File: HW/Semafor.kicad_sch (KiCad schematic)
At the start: 62 parts, among them J1 USB_C_Receptacle_USB2.0, J2 USB_plug, M1 Motor_DC, Q3 Q_NMOS_GSD, Q4 Q_NMOS_GSD, SW6 SW_SPDT, U1 ESP32-C3, U2 CN3058E, U3 LT1930, U4 E22-900T22D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

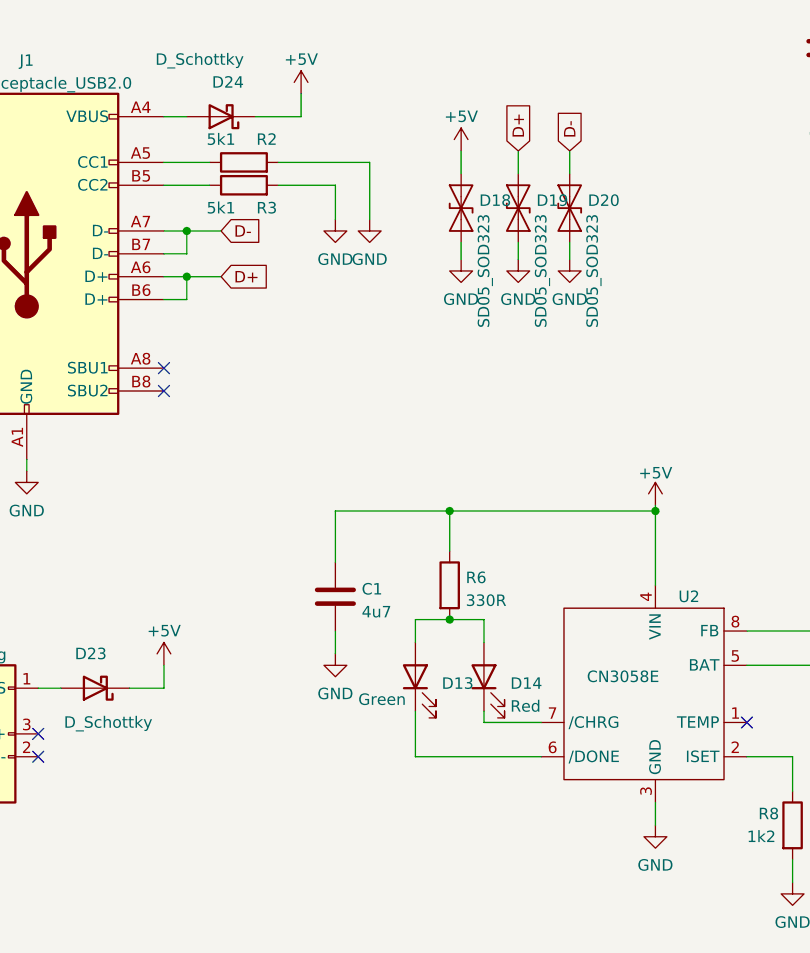
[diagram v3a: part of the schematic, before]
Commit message: routing PCB - LEDs
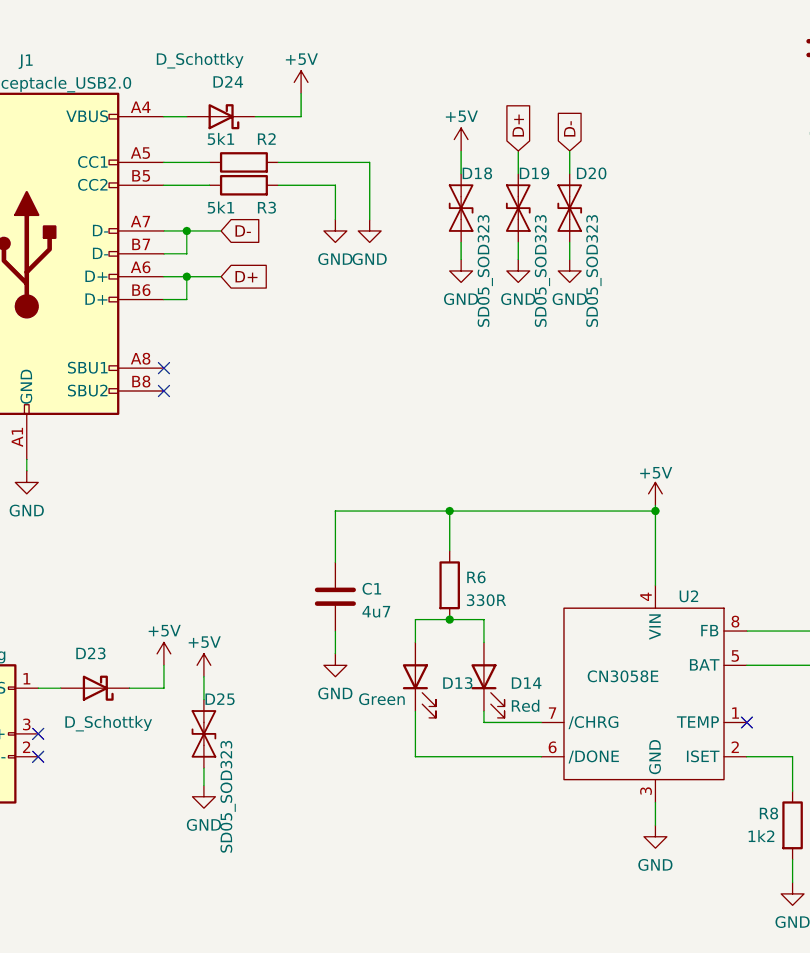
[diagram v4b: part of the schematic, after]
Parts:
- added D25: SD05_SOD323, Diode_SMD:D_SOD-323, symbol Diode:SD05_SOD323
- R2, R3: footprint Resistor_SMD:R_0603_1608Metric -> Resistor_SMD:R_0402_1005Metric
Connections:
- net +5V: now also D25.2 (A2)
- net GND: now also D25.1 (A1)
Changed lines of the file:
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@@
+    (stroke (width 0) (type default) (color 0 0 0 0))
+  )
+  (wire (pts (xy 52.705 176.53) (xy 52.705 178.435))
     (stroke (width 0) (type default) (color 0 0 0 0))
   )
@@
   )
   (wire (pts (xy 123.825 165.1) (xy 138.43 165.1))
+    (stroke (width 0) (type default) (color 0 0 0 0))
+  )
+  (wire (pts (xy 52.705 166.37) (xy 52.705 168.91))
     (stroke (width 0) (type default) (color 0 0 0 0))
   )
@@
   (symbol (lib_id "Diode:SD05_SOD323") (at 93.345 114.3 90) (unit 1)
     (in_bom yes) (on_board yes)
-    (property "Reference" "D20" (id 0) (at 95.3516 113.4653 90)
+    (property "Reference" "D20" (id 0) (at 93.98 110.49 90)
       (effects (font (size 1.27 1.27)) (justify right))
     )
@@
     (pin "1")
   )
+  (symbol (lib_id "power:+5V") (at 52.705 166.37 0) (unit 1)
+    (in_bom yes) (on_board yes)
+    (property "Reference" "#PWR0147" (id 0) (at 52.705 170.18 0)
+      (effects (font (size 1.27 1.27)) hide)
+    )
+    (property "Value" "+5V" (id 1) (at 52.705 162.56 0))
+    (property "Footprint" "" (id 2) (at 52.705 166.37 0)
+      (effects (font (size 1.27 1.27)) hide)
+    )
+    (property "Datasheet" "" (id 3) (at 52.705 166.37 0)
+      (effects (font (size 1.27 1.27)) hide)
+    )
+    (pin "1")
+  )
   (symbol (lib_id "Library:Cap_btn") (at 217.17 43.18 0) (unit 1)
     (in_bom yes) (on_board yes) (fields_autoplaced)
@@
   (symbol (lib_id "Diode:SD05_SOD323") (at 81.28 114.3 90) (unit 1)
     (in_bom yes) (on_board yes)
-    (property "Reference" "D18" (id 0) (at 83.2866 113.4653 90)
+    (property "Reference" "D18" (id 0) (at 81.28 110.49 90)
       (effects (font (size 1.27 1.27)) (justify right))
     )
@@
     (property "Reference" "R3" (id 0) (at 59.69 114.3 90))
     (property "Value" "5k1" (id 1) (at 54.61 114.3 90))
-    (property "Footprint" "Resistor_SMD:R_0603_1608Metric" (id 2) (at 57.15 113.538 90)
+    (property "Footprint" "Resistor_SMD:R_0402_1005Metric" (id 2) (at 57.15 113.538 90)
       (effects (font (size 1.27 1.27)) hide)
     )
@@
     (pin "1")
     (pin "2")
+  )
+  (symbol (lib_id "power:GND") (at 52.705 178.435 0) (unit 1)
+    (in_bom yes) (on_board yes) (fields_autoplaced)
+    (property "Reference" "#PWR0189" (id 0) (at 52.705 184.785 0)
+      (effects (font (size 1.27 1.27)) hide)
+    )
+    (property "Value" "GND" (id 1) (at 52.705 182.8784 0))
+    (property "Footprint" "" (id 2) (at 52.705 178.435 0)
+      (effects (font (size 1.27 1.27)) hide)
+    )
+    (property "Datasheet" "" (id 3) (at 52.705 178.435 0)
+      (effects (font (size 1.27 1.27)) hide)
+    )
+    (pin "1")
   )
   (symbol (lib_id "power:+3V3") (at 138.43 161.29 0) (unit 1)
@@
     (pin "2")
   )
+  (symbol (lib_id "Diode:SD05_SOD323") (at 52.705 172.72 90) (unit 1)
+    (in_bom yes) (on_board yes)
+    (property "Reference" "D25" (id 0) (at 52.705 168.91 90)
+      (effects (font (size 1.27 1.27)) (justify right))
+    )
+    (property "Value" "SD05_SOD323" (id 1) (at 55.245 173.355 0)
+      (effects (font (size 1.27 1.27)) (justify right))
+    )
+    (property "Footprint" "Diode_SMD:D_SOD-323" (id 2) (at 57.785 172.72 0)
+      (effects (font (size 1.27 1.27)) hide)
+    )
+    (property "Datasheet" "https://www.littelfuse.com/~/media/electronics/datasheets/tvs_diode_arrays/littelfuse_tvs_diode_array_sd_c_datasheet.pdf.pdf" (id 3) (at 52.705 172.72 0)
+      (effects (font (size 1.27 1.27)) hide)
+    )
+    (pin "1")
+    (pin "2")
+  )
   (symbol (lib_id "power:GND") (at 262.89 76.2 0) (unit 1)
     (in_bom yes) (on_board yes) (fields_autoplaced)
@@
   (symbol (lib_id "Diode:SD05_SOD323") (at 87.63 114.3 90) (unit 1)
     (in_bom yes) (on_board yes)
-    (property "Reference" "D19" (id 0) (at 89.6366 113.4653 90)
+    (property "Reference" "D19" (id 0) (at 87.63 110.49 90)
       (effects (font (size 1.27 1.27)) (justify right))
     )
@@
     (property "Reference" "R2" (id 0) (at 59.69 106.68 90))
     (property "Value" "5k1" (id 1) (at 54.61 106.68 90))
-    (property "Footprint" "Resistor_SMD:R_0603_1608Metric" (id 2) (at 57.15 110.998 90)
+    (property "Footprint" "Resistor_SMD:R_0402_1005Metric" (id 2) (at 57.15 110.998 90)
       (effects (font (size 1.27 1.27)) hide)
     )
@@
       (reference "#PWR0146") (unit 1) (value "GND") (footprint "")
     )
+    (path "/6f402524-d09a-460a-8ccc-a220f2173d97"
+      (reference "#PWR0147") (unit 1) (value "+5V") (footprint "")
+    )
     (path "/872d82c3-a632-46e9-a03d-bcfba3159600"
       (reference "#PWR0148") (unit 1) (value "GND") (footprint "")
@@
       (reference "#PWR0188") (unit 1) (value "+5V") (footprint "")
     )
+    (path "/88b25ae4-3209-4ef6-972e-af4c0363438a"
+      (reference "#PWR0189") (unit 1) (value "GND") (footprint "")
+    )
     (path "/dc51458a-51c3-4e6e-b128-98c3847d175f"
       (reference "BT1") (unit 1) (value "Battery_Cell") (footprint "Library:battery_dock")
@@
       (reference "D24") (unit 1) (value "D_Schottky") (footprint "Diode_SMD:D_SOD-123")
     )
+    (path "/edaae4c5-e51f-4abe-8951-ccdbb7dd6dd4"
+      (reference "D25") (unit 1) (value "SD05_SOD323") (footprint "Diode_SMD:D_SOD-323")
+    )
     (path "/65e3b0a4-d5bc-4561-b10b-10b1f0c591cf"
       (reference "J1") (unit 1) (value "USB_C_Receptacle_USB2.0") (footprint "Connector_USB:USB_C_Receptacle_HRO_TYPE-C-31-M-12")
@@
     )
     (path "/fa8bfff0-52ba-47ec-8cdd-c865266d5aec"
-      (reference "R2") (unit 1) (value "5k1") (footprint "Resistor_SMD:R_0603_1608Metric")
+      (reference "R2") (unit 1) (value "5k1") (footprint "Resistor_SMD:R_0402_1005Metric")
     )
     (path "/80d9d335-b0b3-4829-b942-61669647ebaf"
-      (reference "R3") (unit 1) (value "5k1") (footprint "Resistor_SMD:R_0603_1608Metric")
+      (reference "R3") (unit 1) (value "5k1") (footprint "Resistor_SMD:R_0402_1005Metric")
     )
     (path "/30c0d7a4-12b9-4537-9b8e-46f5d11bfc2e/cfed6ac4-ecea-46e5-96b2-549bd2f6de6d"

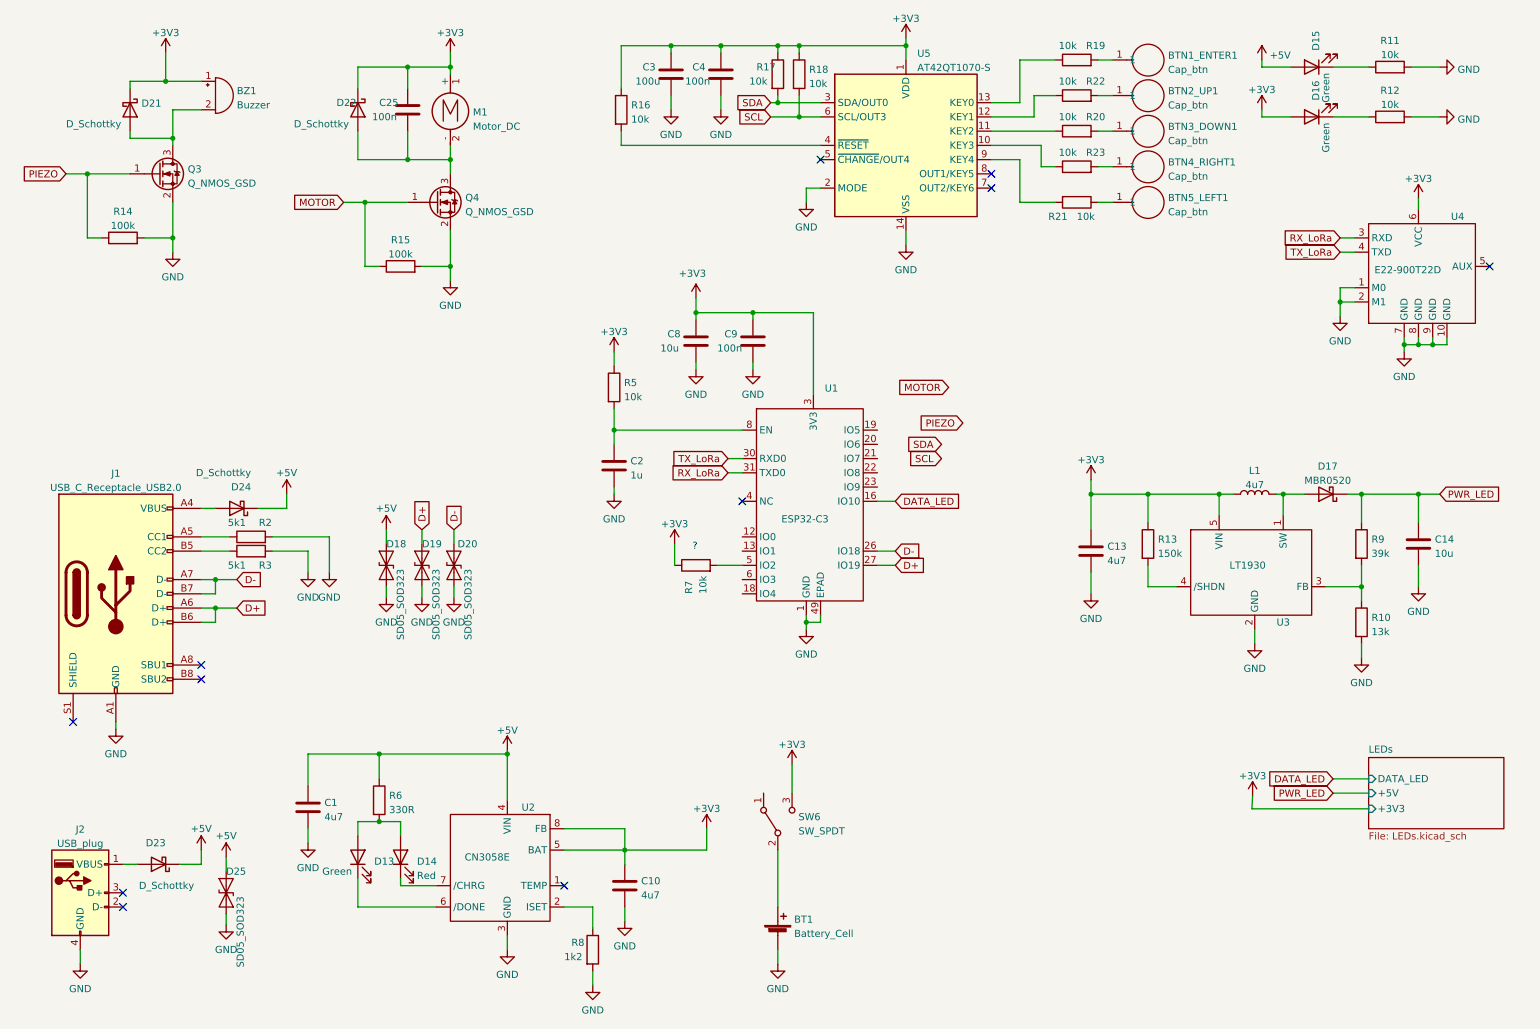
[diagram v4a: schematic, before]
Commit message: add fill of description field
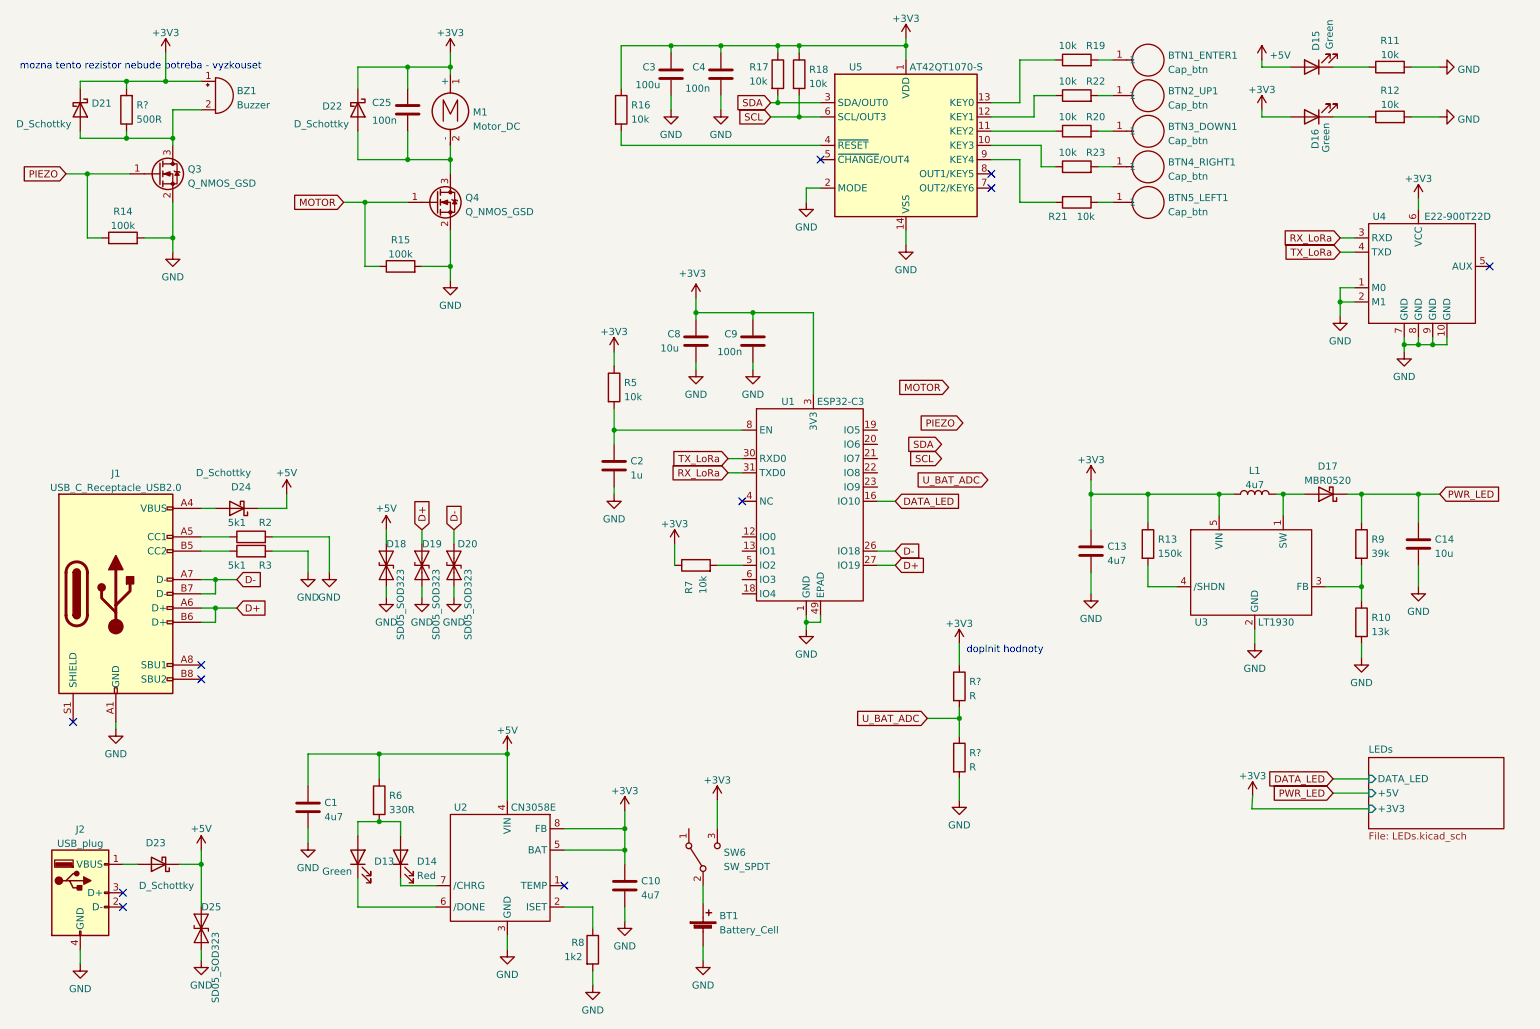
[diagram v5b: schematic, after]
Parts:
- added R?: 500R, Resistor_SMD:R_0603_1608Metric, symbol Device:R
- added R? (x2): R, Resistor_SMD:R_0603_1608Metric, symbol Device:R
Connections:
- net +3V3: now also R?.1, R?.2
- net GND: now also R?.2
- net at BZ1.2 (+), D21.2 (A), Q3.3 (D): now also R?.1
- new net U_BAT_ADC: R?.1, R?.2
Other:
- note added: "doplnit hodnoty"
- note added: "mozna tento rezistor nebude potreba - vyzkouset"
- note removed: "?"
- title: (none) -> Semafor
- moved on the sheet: BT1, D21, D25, SW6

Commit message: add voltage reference
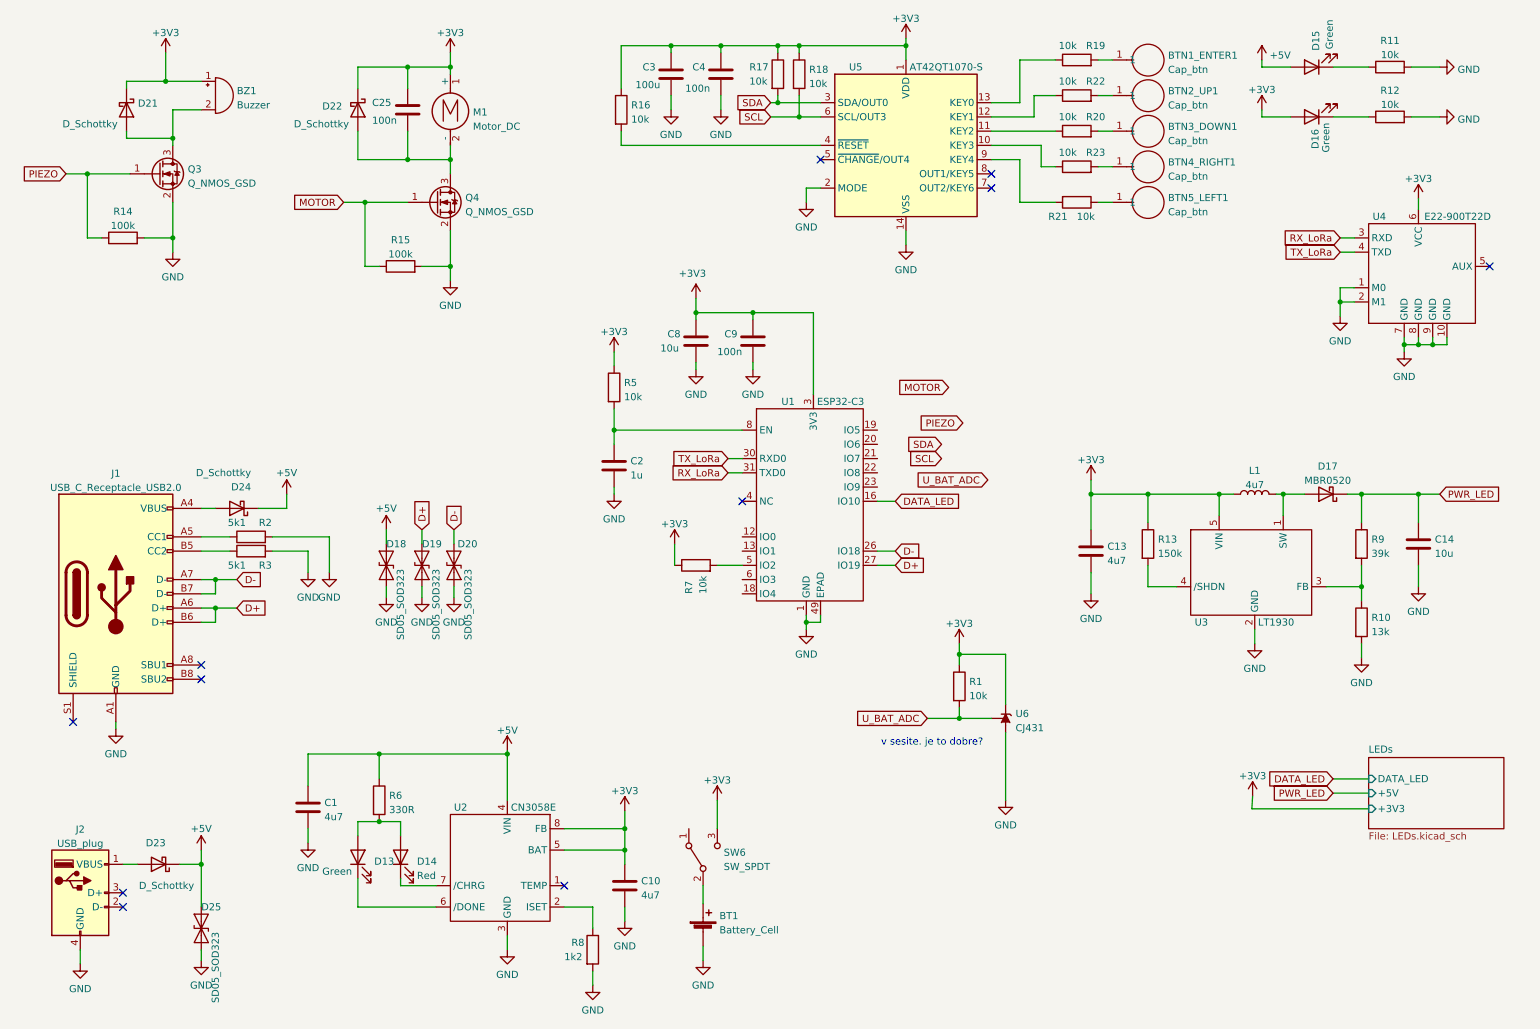
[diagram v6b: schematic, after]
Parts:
- removed R?: 500R, Resistor_SMD:R_0603_1608Metric, symbol Device:R
- removed R?: R, Resistor_SMD:R_0603_1608Metric, symbol Device:R
- added U6: CJ431, Package_TO_SOT_SMD:SOT-23, symbol Reference_Voltage:CJ432
- R1: renamed from R?; value R -> 10k
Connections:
- net +3V3: now also U6.2 (K)
- net GND: now also U6.3 (A)
- net U_BAT_ADC: now also U6.1 (REF)
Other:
- note added: "v sesite. je to dobre?"
- note removed: "doplnit hodnoty"
- note removed: "mozna tento rezistor nebude potreba - vyzkouset"
- moved on the sheet: D21
